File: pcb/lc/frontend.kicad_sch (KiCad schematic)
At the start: 34 parts, among them J1 AudioJack3_Ground_Switch, J2 AudioJack3_Ground_Switch, U4 MCP6004, U5 REF3012

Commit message: * [PCB LC]
  - Change to MCP1501 reference
  - Some retouching of traces
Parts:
- removed U5: REF3012, Package_TO_SOT_SMD:SOT-23, symbol Reference_Voltage:REF3012
- added U1: MCP1501-10xCH, Package_TO_SOT_SMD:SOT-23-6, symbol Reference_Voltage:MCP1501-10xCH
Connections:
- net GND: now also U1.2 (GND), U1.3 (GND), U1.5 (GND)
- net V_REF: now also U1.1 (OUT)
- net at C10.1, R24.1: now also U1.4 (~{SHDN}), U1.6 (VDD)
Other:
- moved on the sheet: C10, C15, R24

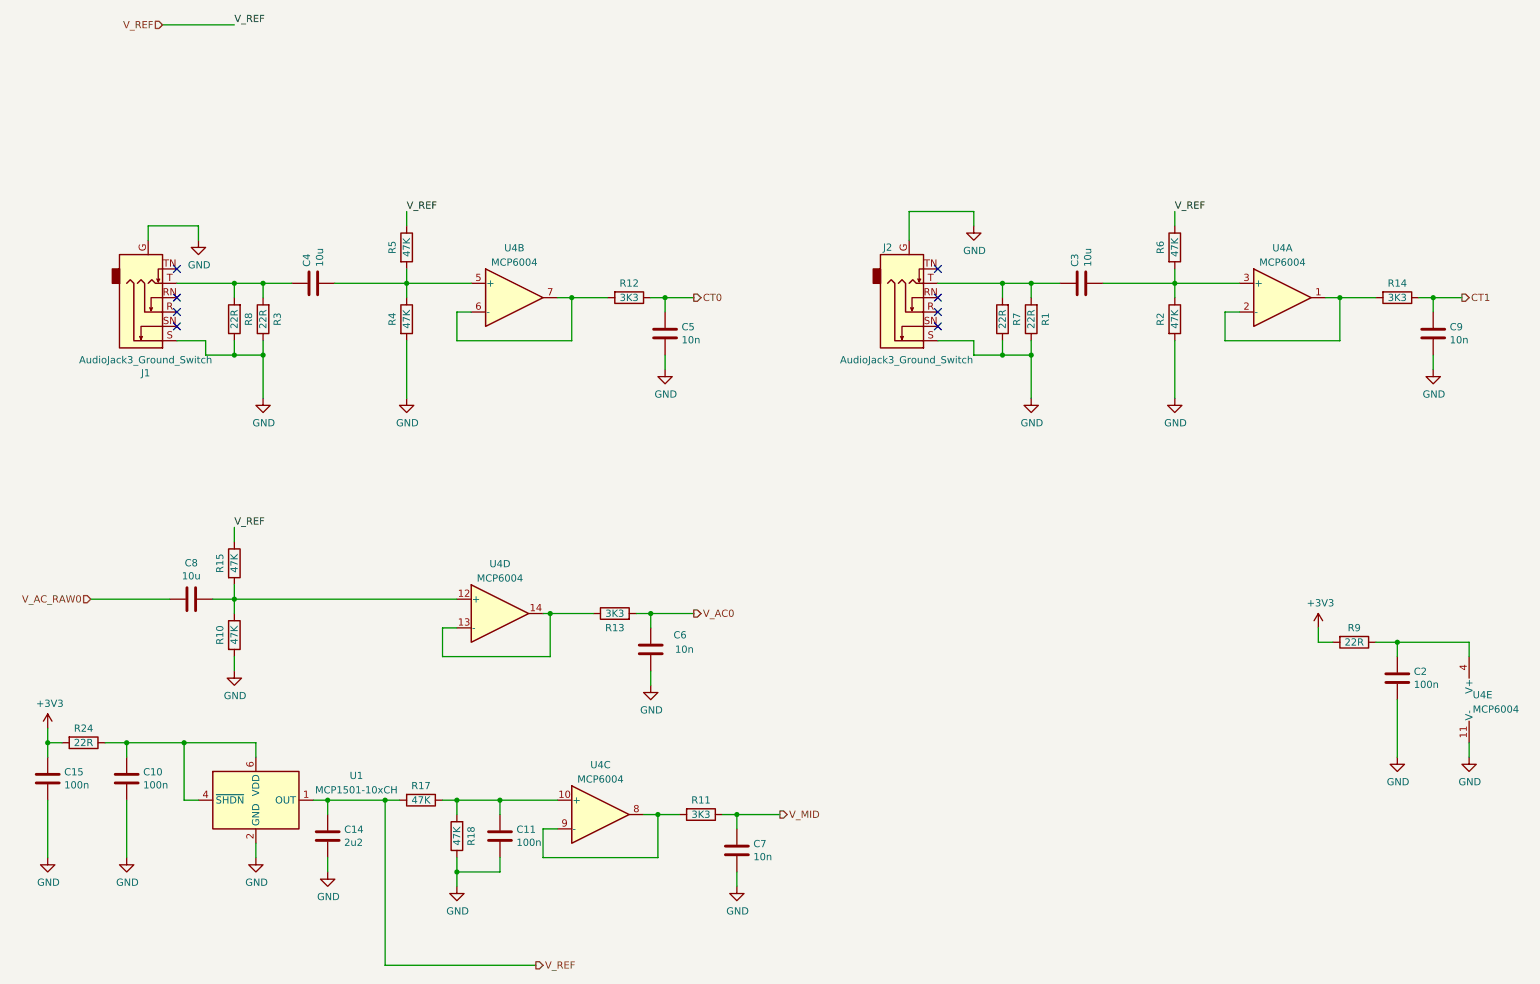
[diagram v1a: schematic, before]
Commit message: * [PCB LC]
  - Revise USB routing/spacing
  - Remove CT current out burden resistors
  - Add AAF filter, revise ADC input filter values
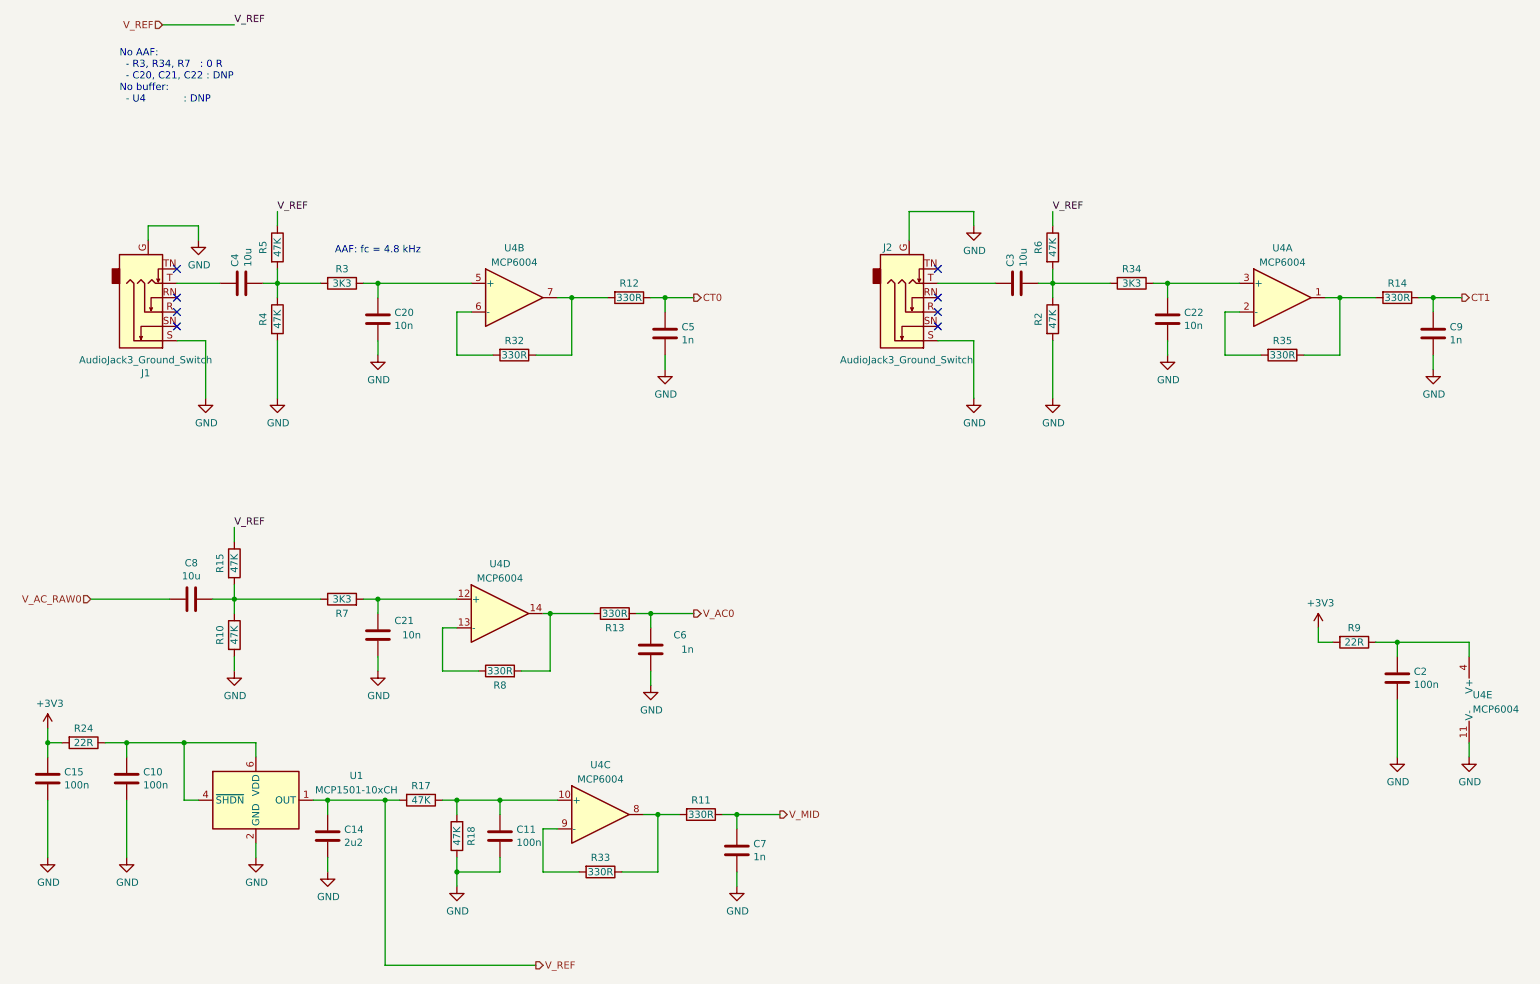
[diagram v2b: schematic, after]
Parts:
- removed R1: 22R, Resistor_SMD:R_0402_1005Metric, symbol Device:R
- added C20, C21, C22: 10n, Capacitor_SMD:C_0402_1005Metric, symbol Device:C
- added R32, R33, R35: 330R, Resistor_SMD:R_0402_1005Metric, symbol Device:R
- added R34: 3K3, Resistor_SMD:R_0402_1005Metric, symbol Device:R
- C5, C6, C7, C9: value 10n -> 1n
- R11, R12, R13, R14: value 3K3 -> 330R
- R3, R7: value 22R -> 3K3
- R8: value 22R -> 330R
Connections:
- net GND: now also C20.1, C21.1, C22.1; no longer R3.1, R7.1, R8.1
- net at C3.2, J2.T: no longer R7.2
- net at R11.2, U4.8: now also R33.1; no longer U4.9 (-)
- net at C8.1, R10.1, R15.2: now also R7.1; no longer U4.12 (+)
- net at C4.2, J1.T: no longer R3.2, R8.2
- net at R14.2, U4.1: now also R35.1; no longer U4.2 (-)
- net at C3.1, R2.1, R6.2: now also R34.2; no longer U4.3 (+)
- net at R13.1, U4.14: now also R8.2; no longer U4.13 (-)
- net at R12.2, U4.7: now also R32.1; no longer U4.6 (-)
- net at C4.1, R4.1, R5.2: now also R3.2; no longer U4.5 (+)
- new net: C22.2, R34.1, U4.3 (+)
- new net: R32.2, U4.6 (-)
- new net: R35.2, U4.2 (-)
- new net: C21.2, R7.2, U4.12 (+)
- new net: R8.1, U4.13 (-)
- new net: C20.2, R3.1, U4.5 (+)
- new net: R33.2, U4.9 (-)
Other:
- note added: "AAF: fc = 4.8 kHz"
- note added: "No AAF: - R3, R34, R7 : 0 R - C20, C21, C22 : DNP No buffer: - U4 : DNP"
- moved on the sheet: C3, C4, R2, R4, R5, R6

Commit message: * [PCB LC]
  - Fix opamp bypass
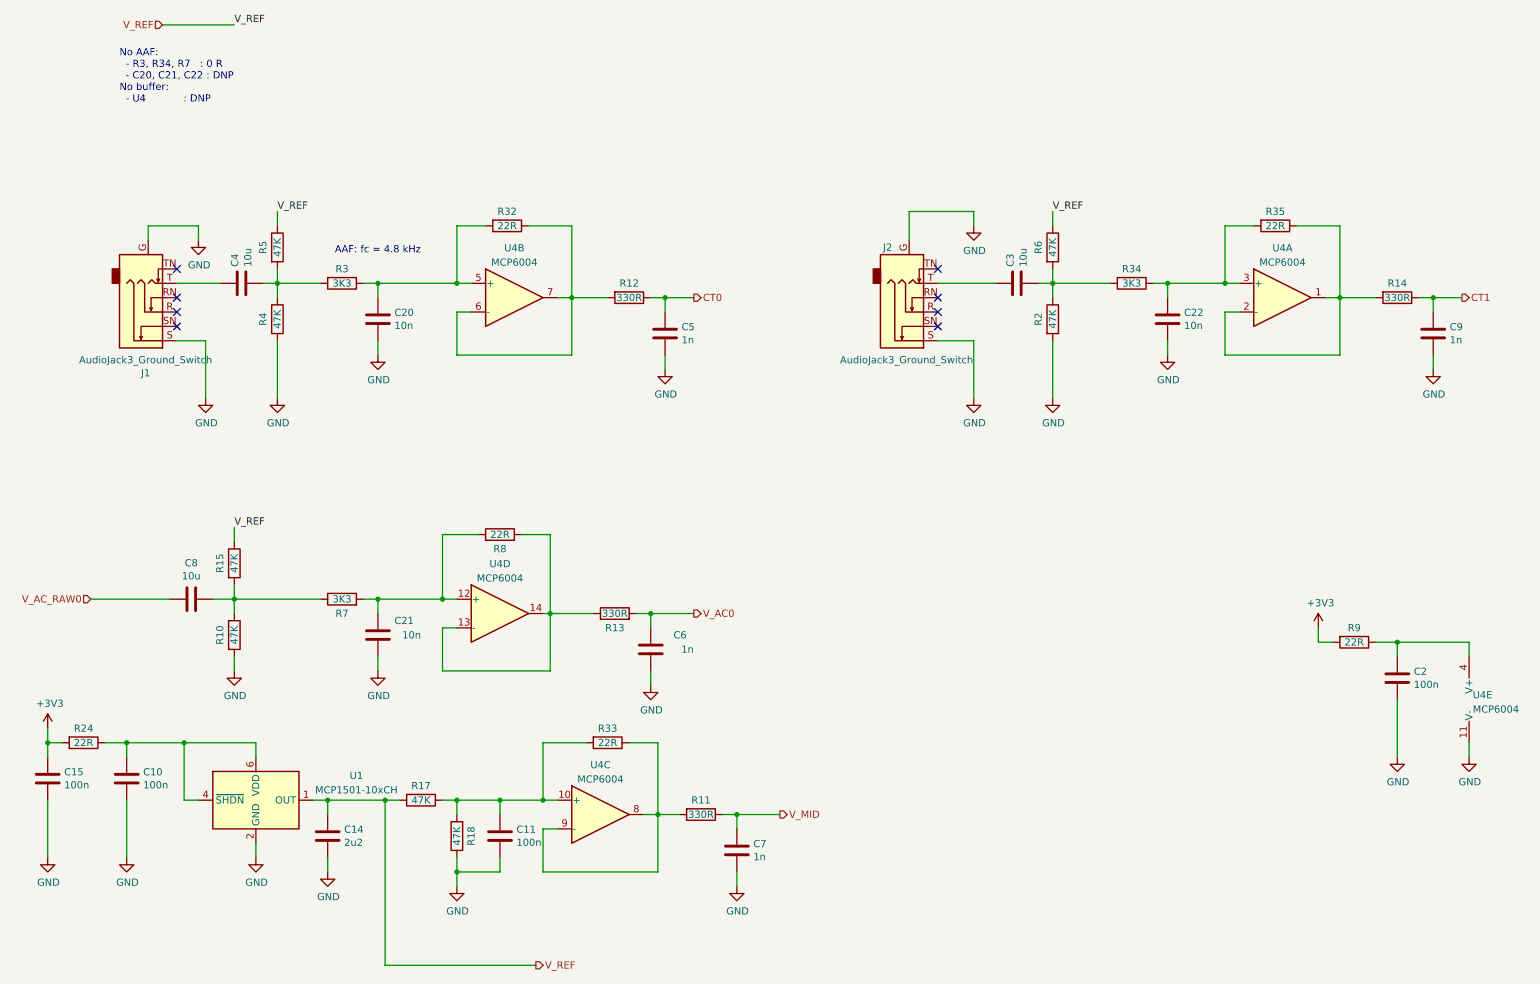
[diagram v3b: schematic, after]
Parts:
- R32, R33, R35, R8: value 330R -> 22R
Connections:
- net at C11.1, R17.1, R18.2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: now also R33.2
- net at C22.2, R34.1, U4.3 (+): now also R35.2
- net at R12.2, R32.1, U4.7: now also U4.6 (-)
- net at R32.2: now also C20.2, R3.1, U4.5 (+); no longer U4.6 (-)
- net at R11.2, R33.1, U4.8: now also U4.9 (-)
- net at R14.2, R35.1, U4.1: now also U4.2 (-)
- net at C21.2, R7.2, U4.12 (+): now also R8.1
- net at U4.13 (-): now also R13.1, R8.2, U4.14; no longer R8.1
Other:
- moved on the sheet: R32, R33, R35, R8

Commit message: * [PCB LC]
  - Bump to KiCad 7
  - Recalculate ADC input RC filter
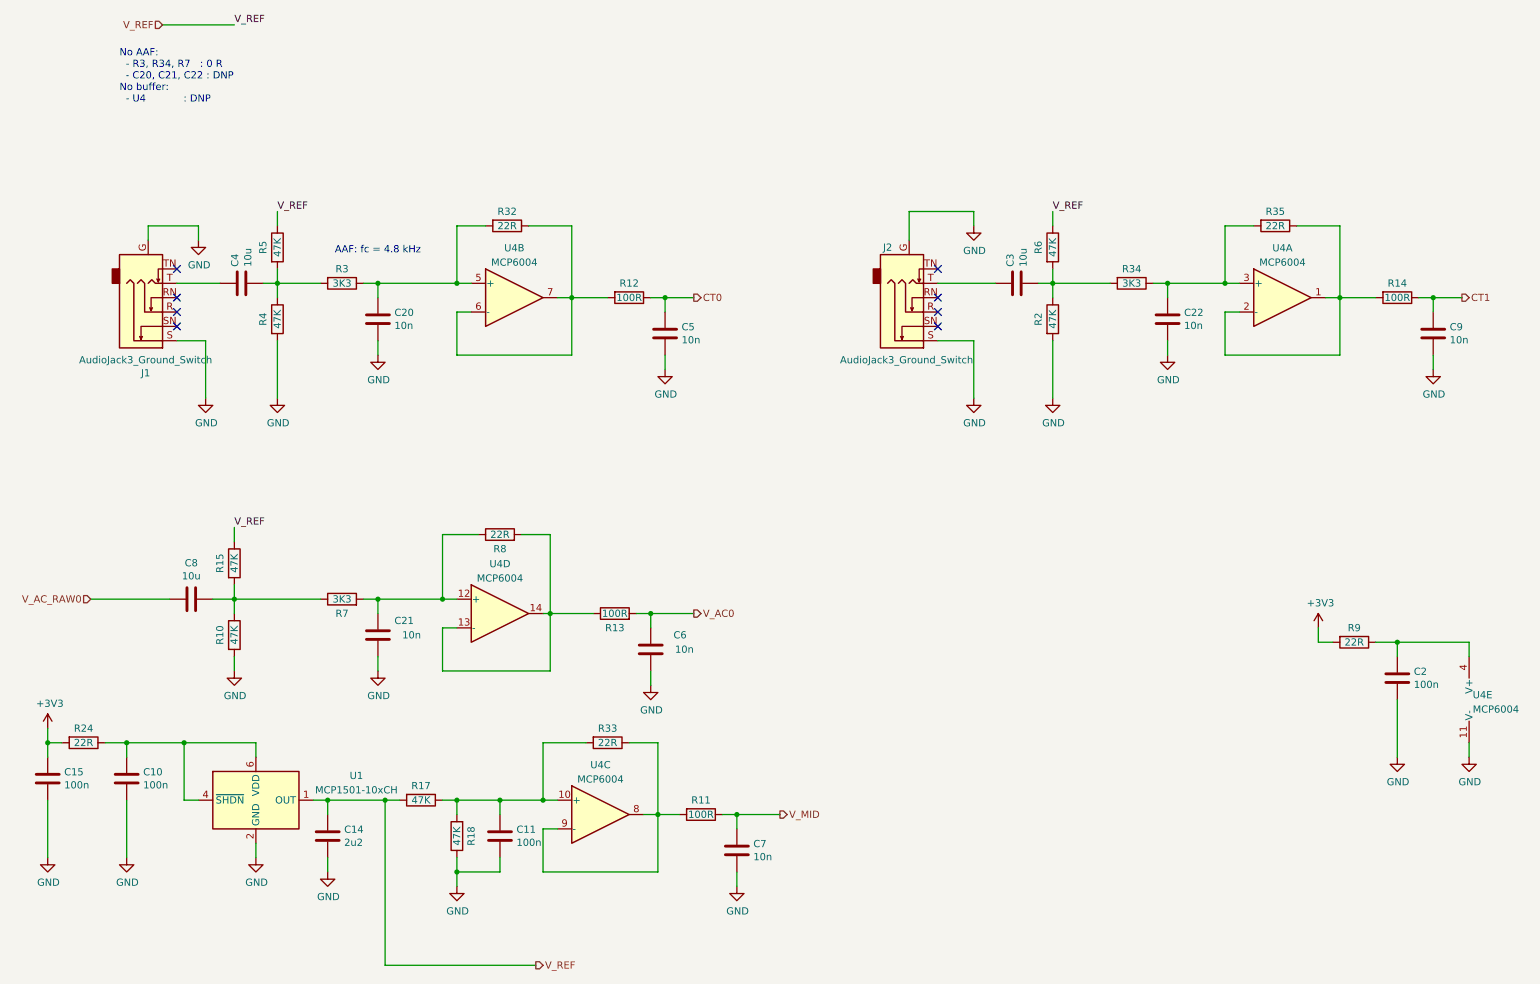
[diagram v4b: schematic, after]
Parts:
- C5, C6, C7, C9: value 1n -> 10n
- R11, R12, R13, R14: value 330R -> 100R

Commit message: * [PCB LC]
  - First iteration of changes from LC-0.1dev -> LC-0.1
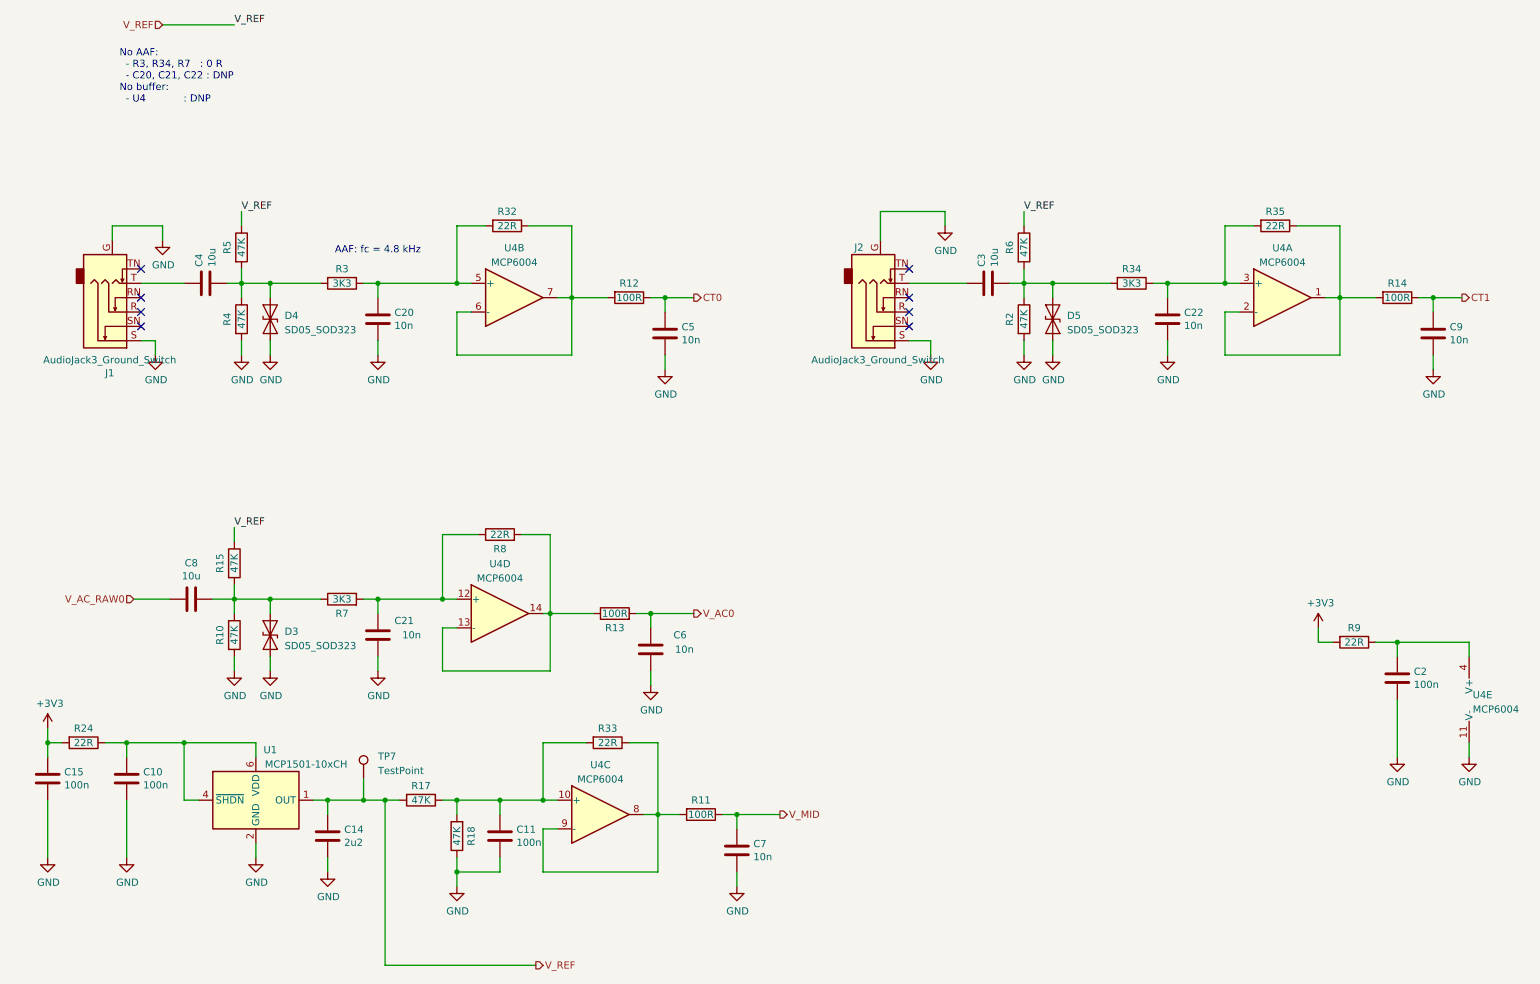
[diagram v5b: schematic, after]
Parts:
- added D3, D4, D5: SD05_SOD323, Diode_SMD:D_SOD-323, symbol Diode:SD05_SOD323
- added TP7: TestPoint, TestPoint:TestPoint_Pad_D1.5mm, symbol Connector:TestPoint
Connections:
- net GND: now also D3.1 (A1), D4.1 (A1), D5.1 (A1)
- net V_REF: now also TP7.1
- net at C8.1, R10.1, R15.2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: now also D3.2 (A2)
- net at C4.1, R3.2, R4.1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: now also D4.2 (A2)
- net at C3.1, R2.1, R34.2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: now also D5.2 (A2)
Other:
- company: (none) -> Tilt Ltd
- title: (none) -> emon32 Low Cost
- moved on the sheet: C3, C4, J1, J2, R2, R4, R5, R6
